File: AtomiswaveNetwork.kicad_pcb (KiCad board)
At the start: 2 copper layers, 41.1 x 22.9 mm, 2 parts, among them U1 LAN_PCB_Connector, U2 G2_FFC

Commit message: First PCB Revision
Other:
- board size 41.1 x 22.9 mm -> 41.1 x 23.1 mm
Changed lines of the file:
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@@
     (pad "50" thru_hole circle (at 29.21 6.6 180) (size 1.2 1.2) (drill 0.8) (layers *.Cu *.Mask))
   )
-  (gr_line (start 126.746 99.314) (end 126.746 76.454) (layer "Edge.Cuts") (width 0.1))
+  (gr_line (start 126.746 99.568) (end 126.746 76.454) (layer "Edge.Cuts") (width 0.1))
   (gr_line (start 160.782 88.392) (end 159.766 87.376) (layer "Edge.Cuts") (width 0.1))
-  (gr_line (start 167.894 99.314) (end 126.746 99.314) (layer "Edge.Cuts") (width 0.1))
+  (gr_line (start 167.894 99.568) (end 126.746 99.568) (layer "Edge.Cuts") (width 0.1))
   (gr_line (start 167.894 88.392) (end 160.782 88.392) (layer "Edge.Cuts") (width 0.1))
   (gr_line (start 159.766 76.454) (end 159.766 87.376) (layer "Edge.Cuts") (width 0.1))
   (gr_line (start 126.746 76.454) (end 159.766 76.454) (layer "Edge.Cuts") (width 0.1))
-  (gr_line (start 167.894 88.392) (end 167.894 99.314) (layer "Edge.Cuts") (width 0.1))
+  (gr_line (start 167.894 88.392) (end 167.894 99.568) (layer "Edge.Cuts") (width 0.1))
   (via (at 160.02 88.9) (size 0.5) (drill 0.3) (layers "F.Cu" "B.Cu") (free) (net 1))
   (via (at 157.48 83.82) (size 0.5) (drill 0.3) (layers "F.Cu" "B.Cu") (free) (net 1))
@@
   (segment (start 142.506 89.25846) (end 143.43748 90.189941) (width 0.2) (layer "F.Cu") (net 12))
   (segment (start 143.43748 93.56748) (end 143.51 93.64) (width 0.2) (layer "F.Cu") (net 12))
-  (segment (start 146.006 88.957136) (end 148.59 91.541136) (width 0.2) (layer "F.Cu") (net 13))
+  (segment (start 148.25 93.64) (end 148.59 93.64) (width 0.2) (layer "F.Cu") (net 13))
+  (segment (start 146.493489 89.444625) (end 146.493489 91.883489) (width 0.2) (layer "F.Cu") (net 13))
   (segment (start 146.006 81.28) (end 146.006 88.957136) (width 0.2) (layer "F.Cu") (net 13))
-  (segment (start 148.59 91.541136) (end 148.59 93.64) (width 0.2) (layer "F.Cu") (net 13))
+  (segment (start 146.493489 91.883489) (end 148.25 93.64) (width 0.2) (layer "F.Cu") (net 13))
+  (segment (start 146.006 88.957136) (end 146.493489 89.444625) (width 0.2) (layer "F.Cu") (net 13))
   (segment (start 134.176511 95.114625) (end 133.793489 95.497647) (width 0.2) (layer "F.Cu") (net 14))
   (segment (start 133.006 81.28) (end 133.006 90.994864) (width 0.2) (layer "F.Cu") (net 14))
@@
   (segment (start 142.006 81.28) (end 142.006 89.22023) (width 0.2) (layer "F.Cu") (net 24))
   (segment (start 142.683489 93.297647) (end 142.683489 95.114625) (width 0.2) (layer "F.Cu") (net 24))
+  (segment (start 150.686511 97.112353) (end 148.932353 98.866511) (width 0.2) (layer "F.Cu") (net 25))
+  (segment (start 150.686511 95.497647) (end 150.686511 97.112353) (width 0.2) (layer "F.Cu") (net 25))
   (segment (start 150.276432 95.087568) (end 150.686511 95.497647) (width 0.2) (layer "F.Cu") (net 25))
-  (segment (start 150.686511 97.112353) (end 148.932353 98.866511) (width 0.2) (layer "F.Cu") (net 25))
   (segment (start 149.506 89.917136) (end 150.876 91.287136) (width 0.2) (layer "F.Cu") (net 25))
   (segment (start 150.276432 92.394704) (end 150.276432 95.087568) (width 0.2) (layer "F.Cu") (net 25))
@@
   (segment (start 148.932353 98.866511) (end 146.876511 98.866511) (width 0.2) (layer "F.Cu") (net 25))
   (segment (start 149.506 81.28) (end 149.506 89.917136) (width 0.2) (layer "F.Cu") (net 25))
-  (segment (start 150.686511 95.497647) (end 150.686511 97.112353) (width 0.2) (layer "F.Cu") (net 25))
   (segment (start 145.506 81.28) (end 145.506 89.16423) (width 0.2) (layer "F.Cu") (net 26))
   (segment (start 148.59 94.808864) (end 148.59 98.04) (width 0.2) (layer "F.Cu") (net 26))
-  (segment (start 146.304 92.522864) (end 148.59 94.808864) (width 0.2) (layer "F.Cu") (net 26))
-  (segment (start 145.506 89.16423) (end 146.304 89.96223) (width 0.2) (layer "F.Cu") (net 26))
-  (segment (start 146.304 89.96223) (end 146.304 92.522864) (width 0.2) (layer "F.Cu") (net 26))
+  (segment (start 145.506 89.16423) (end 146.05 89.70823) (width 0.2) (layer "F.Cu") (net 26))
+  (segment (start 146.05 92.268864) (end 148.59 94.808864) (width 0.2) (layer "F.Cu") (net 26))
+  (segment (start 146.05 89.70823) (end 146.05 92.268864) (width 0.2) (layer "F.Cu") (net 26))
   (zone (net 8) (net_name "+3V3") (layer "F.Cu") (hatch edge 0.508)
     (priority 1)
@@
         (xy 160.782 88.392)
         (xy 167.894 88.392)
-        (xy 167.894 99.314)
-        (xy 126.746 99.314)
+        (xy 167.894 99.568)
+        (xy 126.746 99.568)
         (xy 126.746 76.454)
         (xy 159.766 76.454)
@@
         (xy 160.782 88.392)
         (xy 167.894 88.392)
-        (xy 167.894 99.314)
-        (xy 126.746 99.314)
+        (xy 167.894 99.568)
+        (xy 126.746 99.568)
         (xy 126.746 76.454)
         (xy 159.766 76.454)

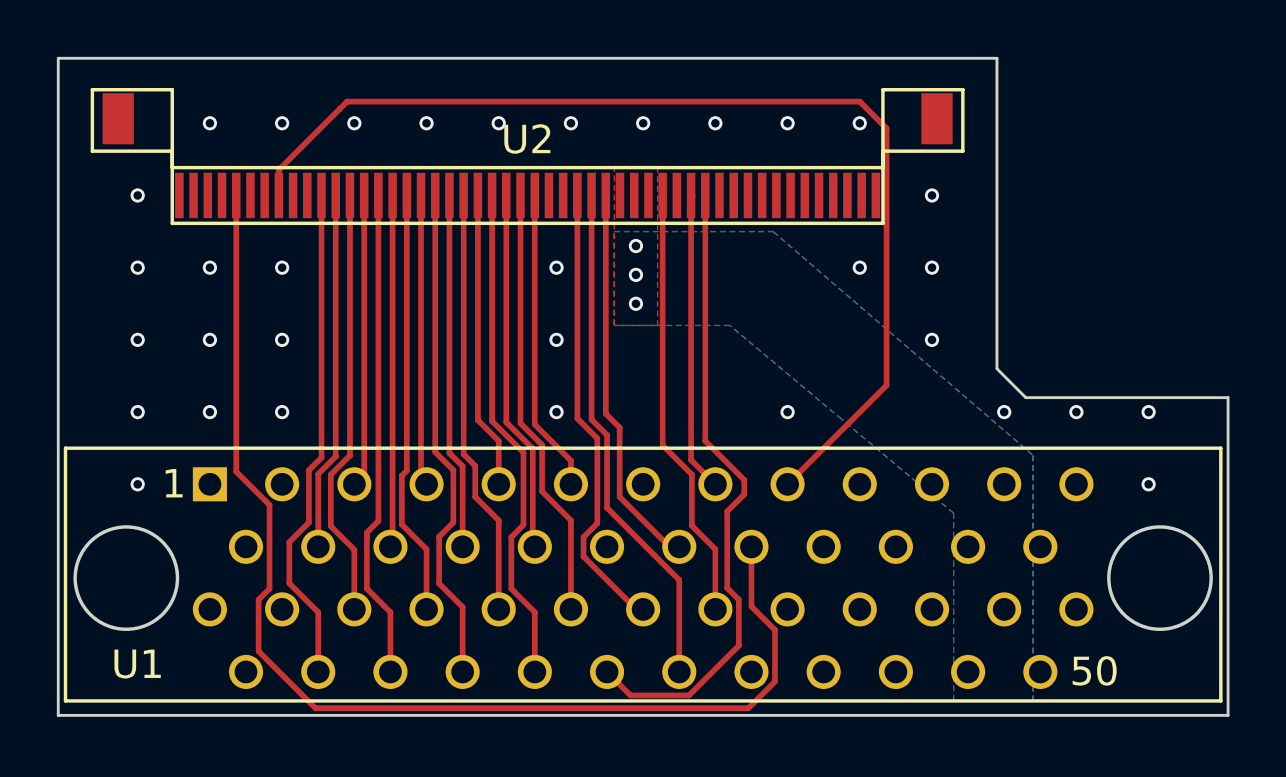
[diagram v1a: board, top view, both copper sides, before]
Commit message: Added version number and exported for manufacture
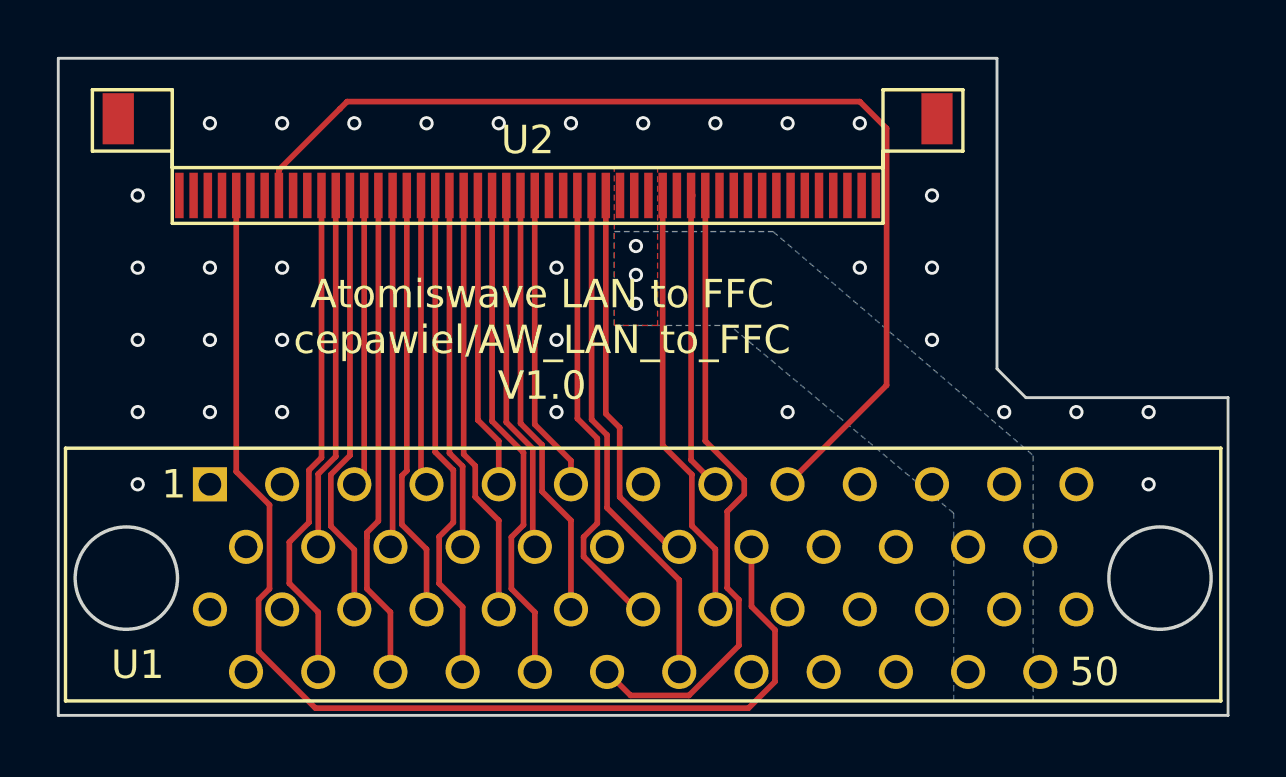
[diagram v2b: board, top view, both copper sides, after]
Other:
- board text added: "Atomiswave LAN to FFC cepawiel/AW_LAN_to_FFC V1.0"
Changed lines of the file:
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@@
     (pad_to_mask_clearance 0)
     (pcbplotparams
-      (layerselection 0x00010fc_ffffffff)
+      (layerselection 0x00010f0_ffffffff)
       (disableapertmacros false)
       (usegerberextensions false)
@@
       (outputformat 1)
       (mirror false)
-      (drillshape 1)
+      (drillshape 0)
       (scaleselection 1)
-      (outputdirectory "")
+      (outputdirectory "plots/")
     )
   )
@@
   (gr_line (start 126.746 76.454) (end 159.766 76.454) (layer "Edge.Cuts") (width 0.1))
   (gr_line (start 167.894 88.392) (end 167.894 99.568) (layer "Edge.Cuts") (width 0.1))
+  (gr_text "Atomiswave LAN to FFC\ncepawiel/AW_LAN_to_FFC\nV1.0" (at 143.764 86.36) (layer "F.SilkS")
+    (effects (font (size 1 1) (thickness 0.15)))
+  )
   (via (at 160.02 88.9) (size 0.5) (drill 0.3) (layers "F.Cu" "B.Cu") (free) (net 1))
   (via (at 157.48 83.82) (size 0.5) (drill 0.3) (layers "F.Cu" "B.Cu") (free) (net 1))

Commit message: Enlarged holes for better fitment on AW LAN Adapter
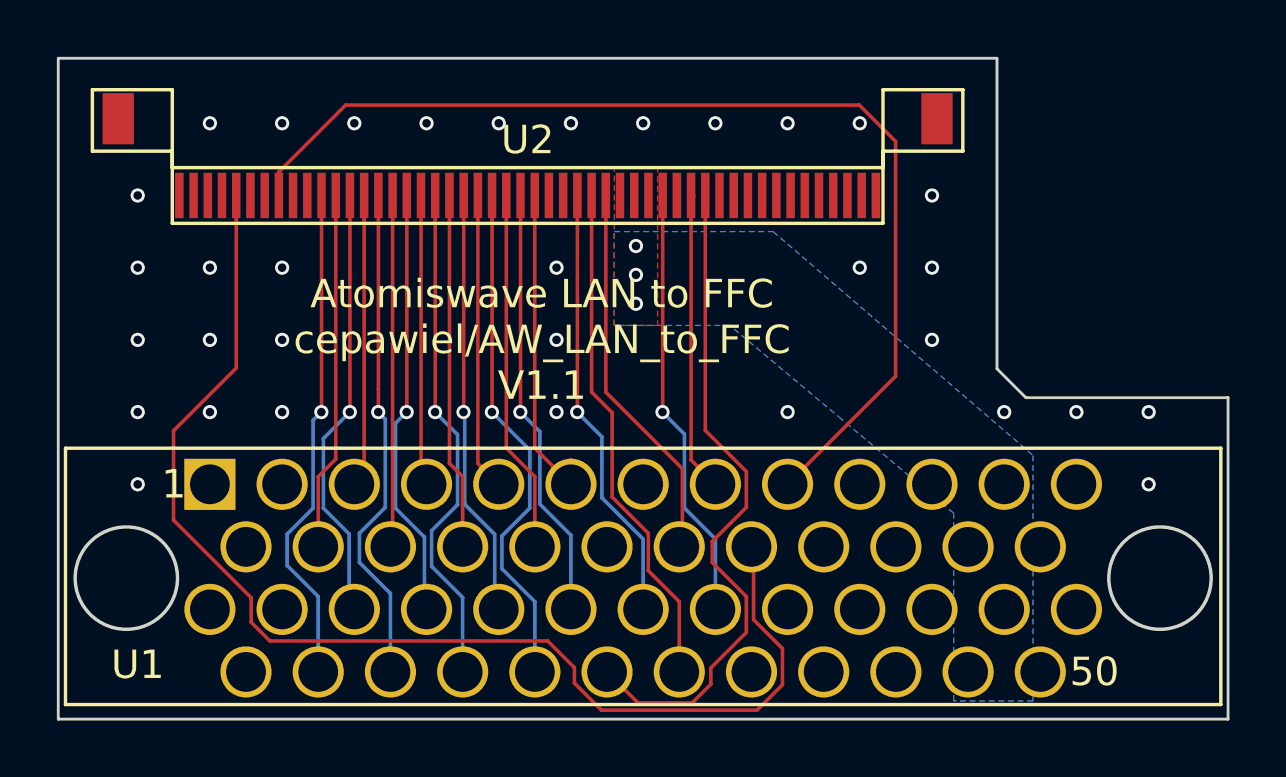
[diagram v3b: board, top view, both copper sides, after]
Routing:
- net /RESET_n: track 41.4 -> 43.3 mm
- net /IRQB_n: track 22.5 -> 23.7 mm
- net /AD15_A7: track 10.7 -> 11.5 mm
- net /AEN_n: track 18.0 -> 18.7 mm
- net /AD12_A4: track 17.7 -> 18.2 mm, vias 0 -> 1
- net /AD4_D4: track 17.3 -> 17.7 mm, vias 0 -> 1
- net /AD8_A0: track 17.6 -> 17.9 mm, vias 0 -> 1
- net /BTA_n: track 16.1 -> 15.8 mm, vias 0 -> 1
- net /AD2_D2: track 15.2 -> 15.4 mm, vias 0 -> 1
- net /AD6_D6: track 15.0 -> 15.2 mm, vias 0 -> 1
- net /AD0_D0: track 17.6 -> 17.7 mm, vias 0 -> 1
- net /AD14_A6: vias 0 -> 1
- net /AD10_A2: vias 0 -> 1
- net /UBE_RD_n: vias 0 -> 1
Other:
- board size 41.1 x 23.1 mm -> 41.1 x 23.2 mm
- board text added: "Atomiswave LAN to FFC cepawiel/AW_LAN_to_FFC V1.1"
- board text removed: "Atomiswave LAN to FFC cepawiel/AW_LAN_to_FFC V1.0"
